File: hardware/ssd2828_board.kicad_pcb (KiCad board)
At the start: 4 copper layers, 91.3 x 35.4 mm, 127 parts, among them IC1 TLV62568DBVR, IC2 MIC5501-3.0YM5-TR, IC3 TPS65131TRGERQ1, J1 FH35C-25S-0.3SHW_50_, J2 FH35C-25S-0.3SHW_50_, J3 Conn_01x34, J4 245863050104829+, J5 503548-1220, J8 FH35C-25S-0.3SHW_50_, U1 SSD2828QN4, U2 PAM2306DYPAA, U3 MIC3289, U4 LP3320, Y1 24mhz

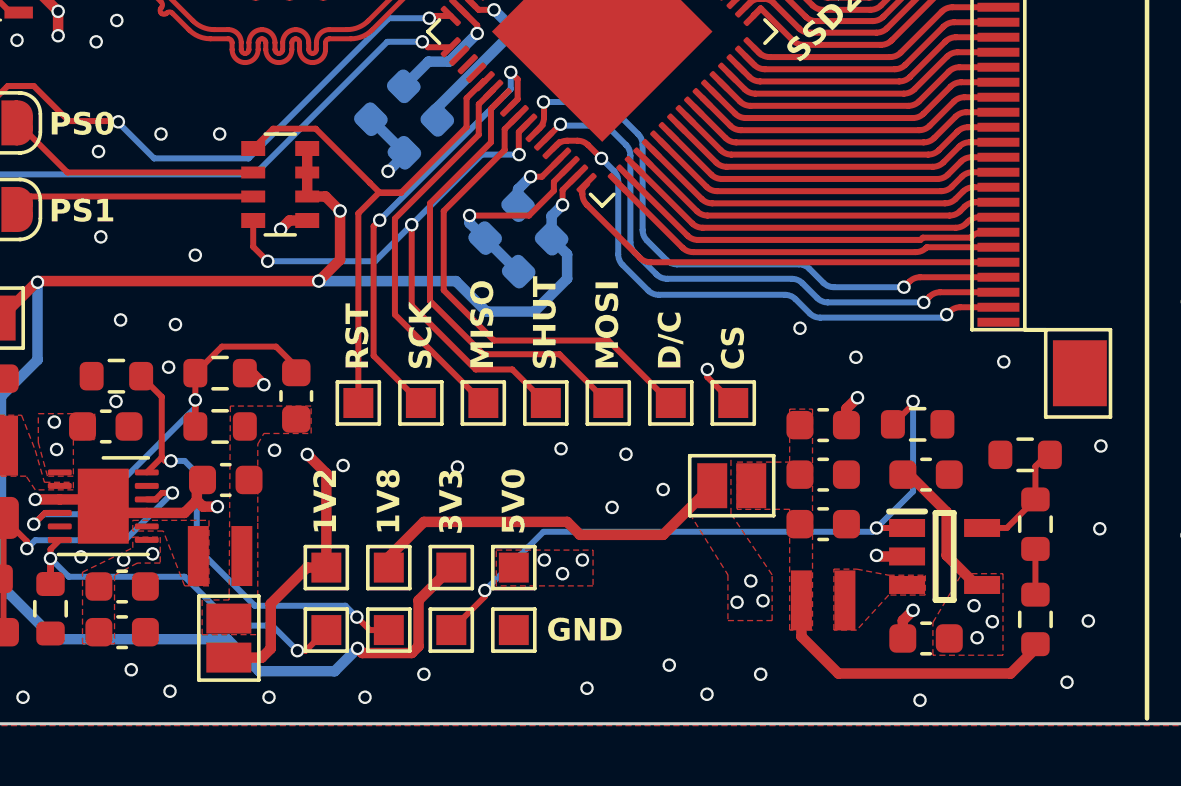
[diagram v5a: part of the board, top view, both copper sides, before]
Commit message: changed the order of pins on the rgb connector + removed a pin from the schematic symbol
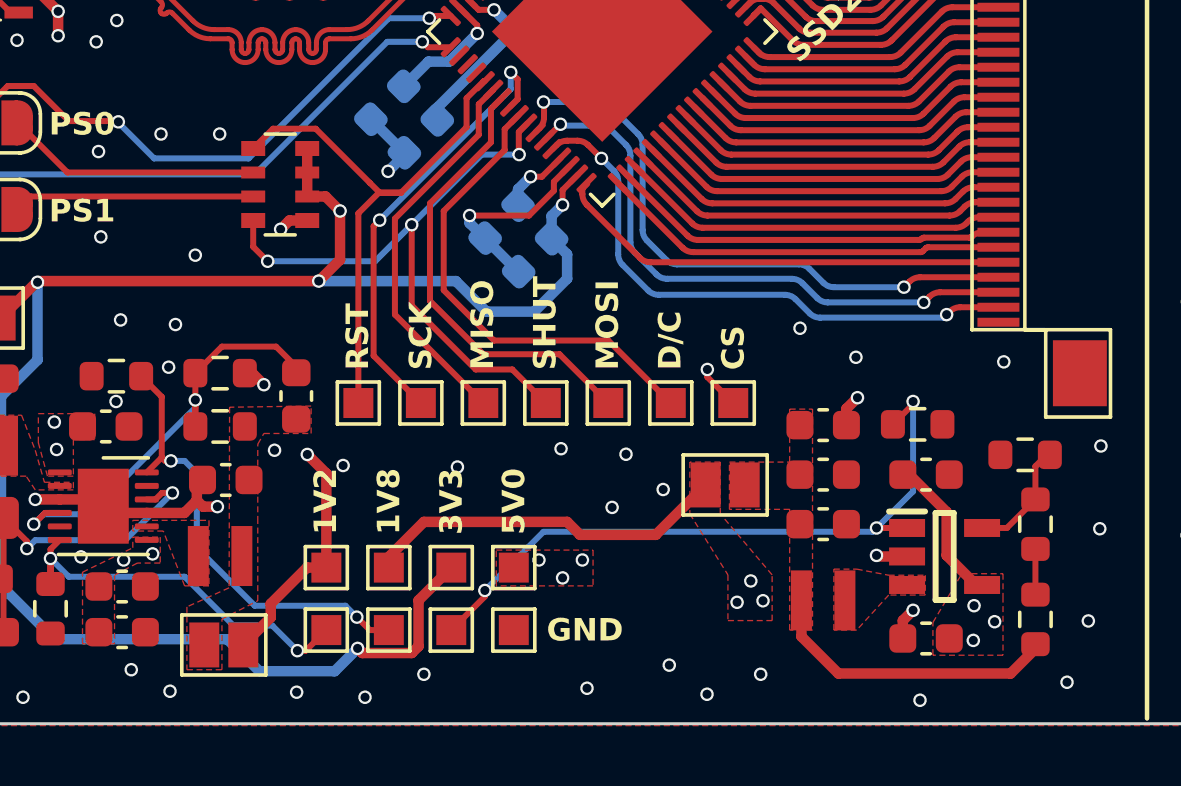
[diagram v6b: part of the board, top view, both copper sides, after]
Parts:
- moved JP5 0.28 mm to (63.5, 83.9), turned to 0 degrees
- moved JP3 0.22 mm to (80.2, 78.6)
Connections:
- J3 pad 10: /SSD2828/RGB_R4 -> /SSD2828/RGB_B4
- J3 pad 11: /SSD2828/RGB_R5 -> /SSD2828/RGB_B5
- J3 pad 12: /SSD2828/RGB_R6 -> /SSD2828/RGB_B6
- J3 pad 13: /SSD2828/RGB_R7 -> /SSD2828/RGB_B7
- J3 pad 22: /SSD2828/RGB_B0 -> /SSD2828/RGB_R0
- J3 pad 23: /SSD2828/RGB_B1 -> /SSD2828/RGB_R1
- J3 pad 24: /SSD2828/RGB_B2 -> /SSD2828/RGB_R2
- J3 pad 25: /SSD2828/RGB_B3 -> /SSD2828/RGB_R3
- J3 pad 26: /SSD2828/RGB_B4 -> /SSD2828/RGB_R4
- J3 pad 27: /SSD2828/RGB_B5 -> /SSD2828/RGB_R5
- J3 pad 28: /SSD2828/RGB_B6 -> /SSD2828/RGB_R6
- J3 pad 29: /SSD2828/RGB_B7 -> /SSD2828/RGB_R7
- J3 pad 6: /SSD2828/RGB_R0 -> /SSD2828/RGB_B0
- J3 pad 7: /SSD2828/RGB_R1 -> /SSD2828/RGB_B1
- J3 pad 8: /SSD2828/RGB_R2 -> /SSD2828/RGB_B2
- J3 pad 9: /SSD2828/RGB_R3 -> /SSD2828/RGB_B3
- U1 pad 35: /SSD2828/RGB_R0 -> /SSD2828/RGB_B0
- U1 pad 36: /SSD2828/RGB_R1 -> /SSD2828/RGB_B1
- U1 pad 37: /SSD2828/RGB_R2 -> /SSD2828/RGB_B2
- U1 pad 38: /SSD2828/RGB_R3 -> /SSD2828/RGB_B3
- U1 pad 39: /SSD2828/RGB_R4 -> /SSD2828/RGB_B4
- U1 pad 40: /SSD2828/RGB_R5 -> /SSD2828/RGB_B5
- U1 pad 41: /SSD2828/RGB_R6 -> /SSD2828/RGB_B6
- U1 pad 42: /SSD2828/RGB_R7 -> /SSD2828/RGB_B7
- U1 pad 51: /SSD2828/RGB_B0 -> /SSD2828/RGB_R0
- U1 pad 52: /SSD2828/RGB_B1 -> /SSD2828/RGB_R1
- U1 pad 53: /SSD2828/RGB_B2 -> /SSD2828/RGB_R2
- U1 pad 54: /SSD2828/RGB_B3 -> /SSD2828/RGB_R3
- U1 pad 55: /SSD2828/RGB_B4 -> /SSD2828/RGB_R4
- U1 pad 56: /SSD2828/RGB_B5 -> /SSD2828/RGB_R5
- U1 pad 57: /SSD2828/RGB_B6 -> /SSD2828/RGB_R6
- U1 pad 58: /SSD2828/RGB_B7 -> /SSD2828/RGB_R7
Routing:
- net /SSD2828/RGB_B0: track 8.91 -> 13.7 mm
- net /SSD2828/RGB_R0: track 13.7 -> 8.91 mm
- net /SSD2828/RGB_R1: track 13.4 -> 9.44 mm
- net /SSD2828/RGB_B1: track 9.44 -> 13.4 mm
- net /SSD2828/RGB_R2: track 13.0 -> 9.68 mm
- net /SSD2828/RGB_B2: track 9.68 -> 13.0 mm
- net /SSD2828/RGB_R3: track 12.8 -> 10.00 mm
- net /SSD2828/RGB_B3: track 10.00 -> 12.8 mm
- net /SSD2828/RGB_R4: track 12.5 -> 10.3 mm
- net /SSD2828/RGB_B4: track 10.3 -> 12.5 mm
- net /SSD2828/RGB_R5: track 12.2 -> 10.6 mm
- net /SSD2828/RGB_B5: track 10.6 -> 12.2 mm
- net +1V2: track 57.5 -> 56.2 mm
- net /SSD2828/RGB_R6: track 11.9 -> 10.9 mm
- net /SSD2828/RGB_B6: track 10.9 -> 11.9 mm
